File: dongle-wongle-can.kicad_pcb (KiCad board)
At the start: 2 copper layers, 29.2 x 61 mm, 40 parts, among them J1 MicroLock, J2 PROTO_IO, J3 PROTO_PWR, J4 UART_DEBUG, J5 Conn_ARM_JTAG_SWD_10, J6 PROTO1, J7 PROTO2, SW1 SW_Push, U1 STM32F042F6Px, U2 SN65HVD233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

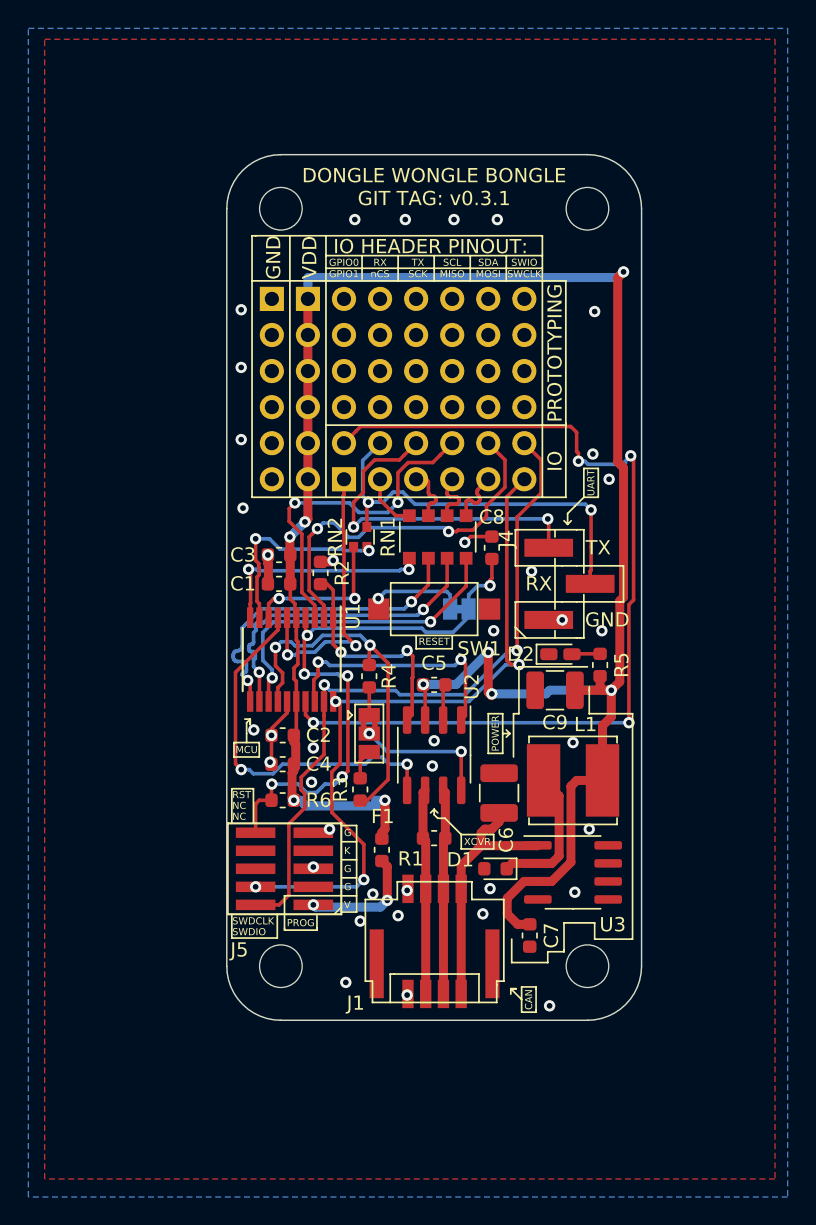
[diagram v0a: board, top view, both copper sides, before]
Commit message: moved some vias off of pads
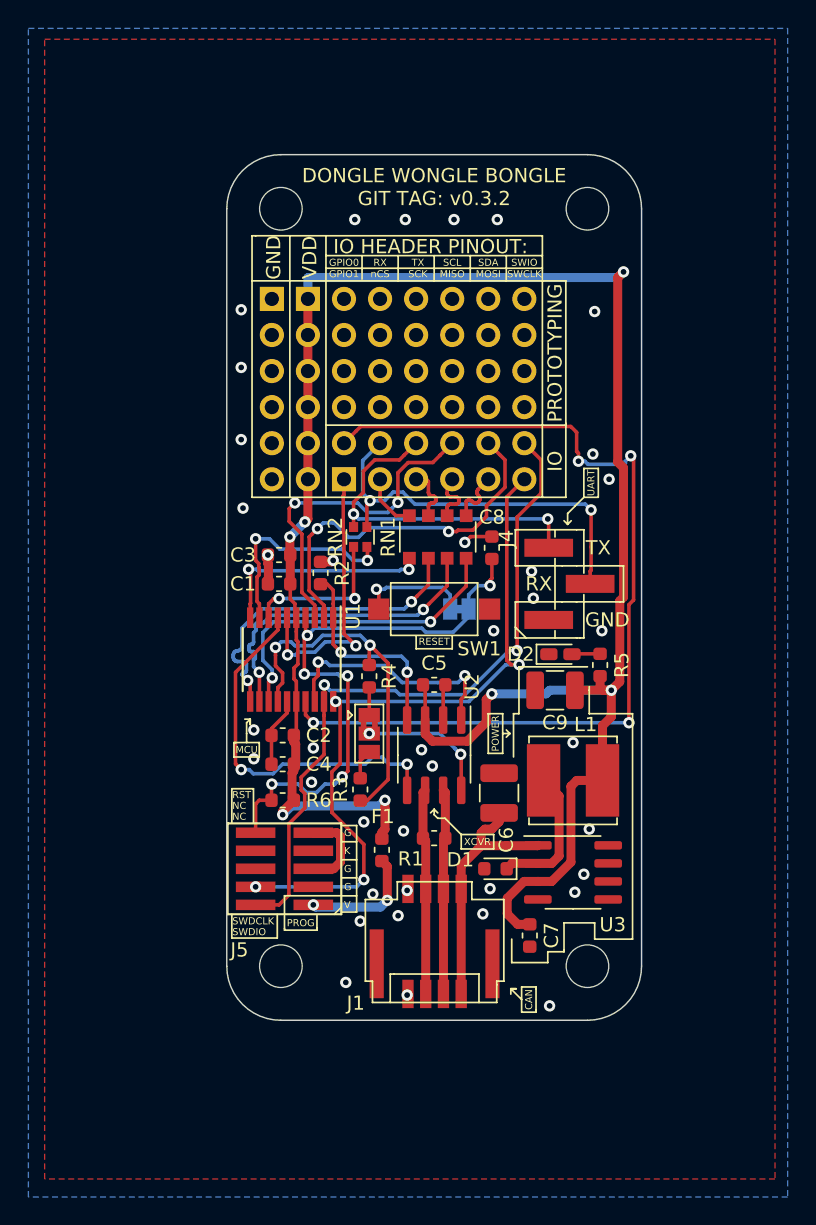
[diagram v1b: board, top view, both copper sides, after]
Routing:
- net GND: track 12.4 -> 18.3 mm
- net Net-(RN2-Pad2): track 14.4 -> 15.6 mm
- net CAN_RX: track 15.8 -> 14.7 mm
- net VDD: track 147.9 -> 148.8 mm, vias 9 -> 7
- net Net-(JP1-Pad1): track 7.14 -> 7.93 mm
- net CAN_TX: track 17.8 -> 17.3 mm
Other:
- board text added: "DONGLE WONGLE BONGLE GIT TAG: v0.3.2"
- board text removed: "DONGLE WONGLE BONGLE GIT TAG: v0.3.1"

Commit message: added protection diode, and fixed jason's OCD
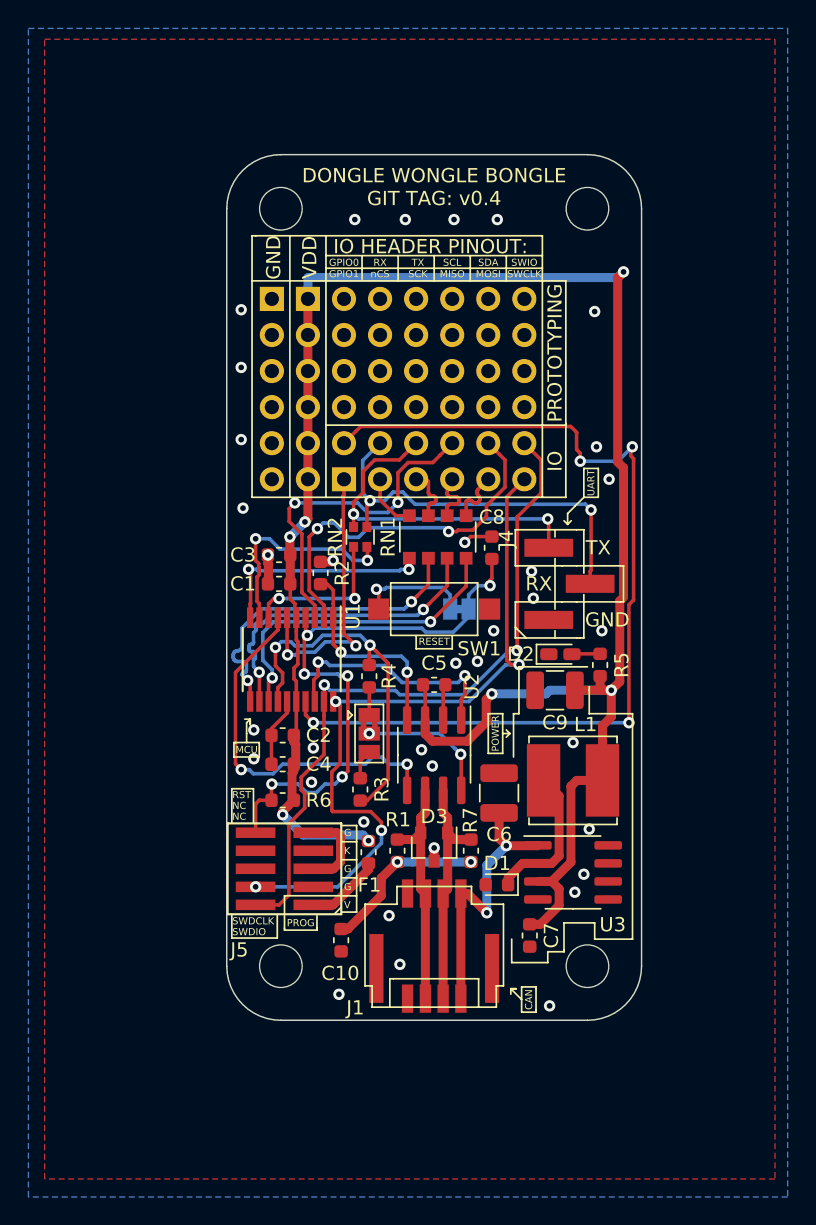
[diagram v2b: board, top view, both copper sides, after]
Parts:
- added C10: 100n, Capacitor_SMD:C_0603_1608Metric, F.Cu at (143.3, 159.5)
- added D3: NUP2105L, Package_TO_SOT_SMD:SOT-23, F.Cu at (149.9, 152.9)
- added R7: 62, Resistor_SMD:R_0603_1608Metric, F.Cu at (152.5, 153.2)
- R1: value DNP -> 62
- moved R1 2.74 mm to (147.3, 153.2), turned to 90 degrees
- moved D1 1.12 mm to (154.3, 155.5)
- moved F1 0.95 mm to (145.2, 153.3)
- moved J1 0.33 mm to (151.7, 157.2)
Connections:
- R1 pad 1: CANH -> Net-(C10-Pad2)
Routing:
- net Net-(C10-Pad2): track 0.00 -> 11.9 mm, vias 0 -> 2
- net VDD: track 148.8 -> 144.1 mm
- net Net-(F1-Pad1): track 8.39 -> 5.35 mm, vias 2 -> 0
- net CANH: track 14.5 -> 16.8 mm
- net CANL: track 14.5 -> 16.8 mm
- net SWDCLK: track 50.4 -> 52.2 mm
- net UPOWER: track 18.1 -> 19.8 mm, vias 0 -> 2
- net GND: track 18.3 -> 19.3 mm, vias 39 -> 36
- net GPIO0: track 66.2 -> 66.9 mm
- net Net-(D1-Pad1): track 9.84 -> 10.5 mm
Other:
- board text added: "DONGLE WONGLE BONGLE GIT TAG: v0.4"
- board text removed: "DONGLE WONGLE BONGLE GIT TAG: v0.3.2"
- board text removed: "XCVR"

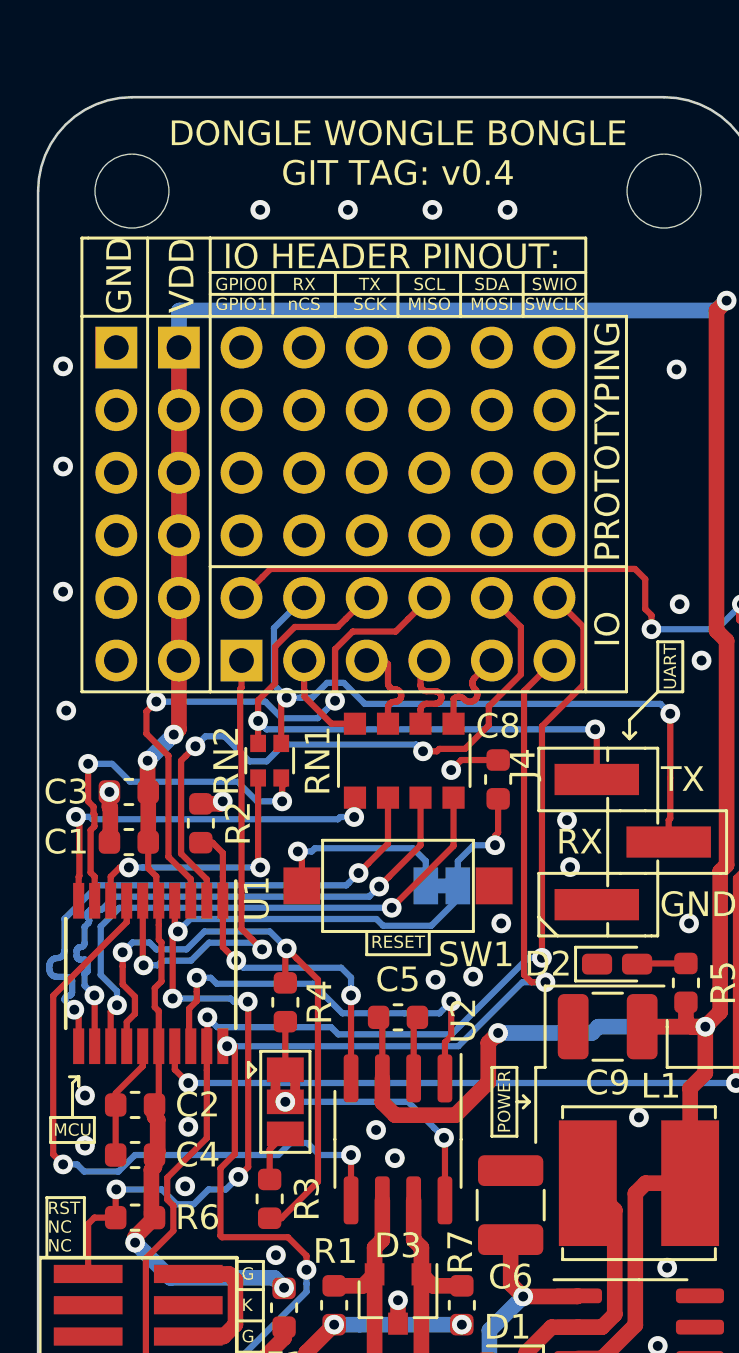
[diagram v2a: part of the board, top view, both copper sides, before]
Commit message: add tp (expensive) on tx and rx
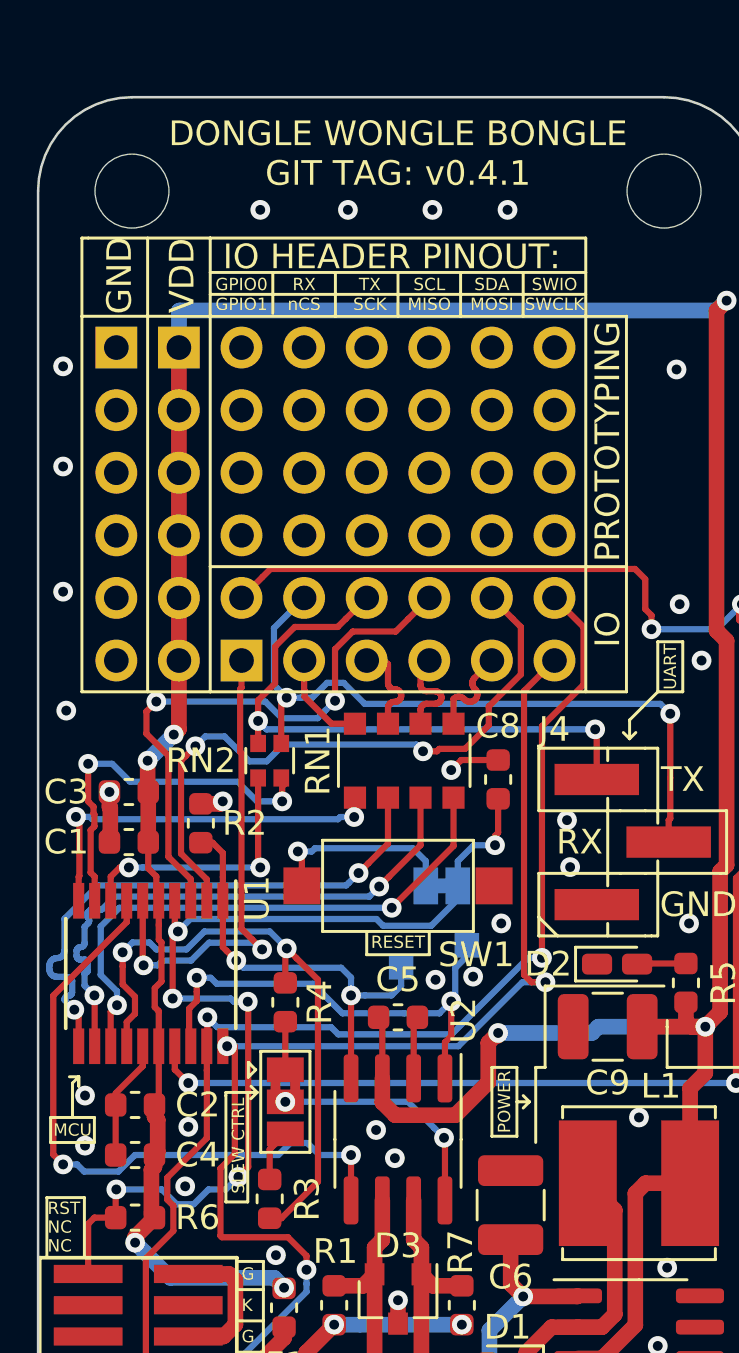
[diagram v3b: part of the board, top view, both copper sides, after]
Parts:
- added TP1: TestPoint, TestPoint:TestPoint_Pad_1.0x1.0mm, B.Cu at (152.7, 138.6)
- added TP2: TestPoint, TestPoint:TestPoint_Pad_1.0x1.0mm, B.Cu at (150.0, 139.4)
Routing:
- net CAN_RX: track 14.7 -> 17.6 mm
- net CAN_TX: track 17.3 -> 19.8 mm
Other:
- board text added: "CAN RX"
- board text added: "CAN TX"
- board text added: "DONGLE WONGLE BONGLE GIT TAG: v0.4.1"
- board text added: "RESET JUMPER CUT BEFORE FLIGHT"
- board text added: "SLEW CTRL"
- board text removed: "DONGLE WONGLE BONGLE GIT TAG: v0.4"
